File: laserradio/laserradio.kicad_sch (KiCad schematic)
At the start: 60 parts, among them J1 USB4105-GF-A, J3 DEBUG, J4 RIGHT, U1 W25Q128JV, U2 RP2040, U3 MCP1702T-3302E_CB, U4 Opamp_Quad, U5 RS2255, U6 AD9837, Y1 12MHz

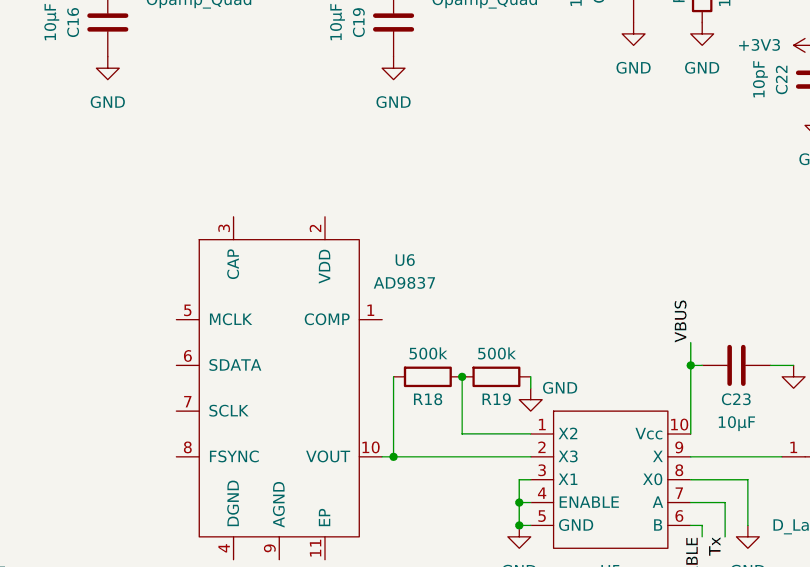
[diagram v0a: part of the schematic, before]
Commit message: swap AD9833 (higher frequency DDS) for AD9837 (lower frequency)
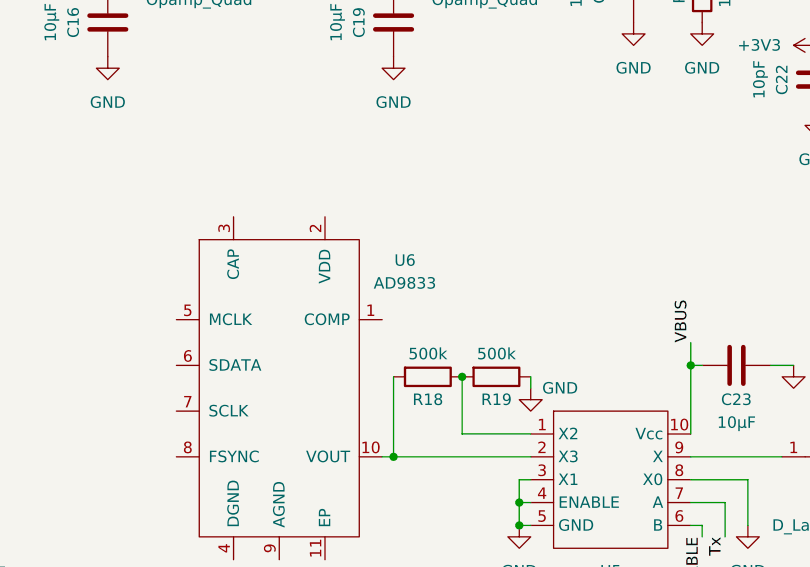
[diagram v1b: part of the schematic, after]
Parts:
- U6: value AD9837 -> AD9833; footprint (none) -> Package_SO:MSOP-10_3x3mm_P0.5mm
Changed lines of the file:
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@@
     (in_bom yes) (on_board yes) (fields_autoplaced)
     (property "Reference" "U6" (id 0) (at 248.92 110.2612 0))
-    (property "Value" "AD9837" (id 1) (at 248.92 112.8012 0))
-    (property "Footprint" "" (id 2) (at 234.95 124.46 0)
-      (effects (font (size 1.27 1.27)) hide)
-    )
-    (property "Datasheet" "" (id 3) (at 234.95 124.46 0)
+    (property "Value" "AD9833" (id 1) (at 248.92 112.8012 0))
+    (property "Footprint" "Package_SO:MSOP-10_3x3mm_P0.5mm" (id 2) (at 234.95 124.46 0)
+      (effects (font (size 1.27 1.27)) hide)
+    )
+    (property "Datasheet" "https://www.analog.com/media/en/technical-documentation/data-sheets/AD9833.pdf" (id 3) (at 234.95 124.46 0)
       (effects (font (size 1.27 1.27)) hide)
     )
@@
     )
     (path "/17770b98-3f4d-46ce-be33-3af9bb07813a"
-      (reference "U6") (unit 1) (value "AD9837") (footprint "")
+      (reference "U6") (unit 1) (value "AD9833") (footprint "Package_SO:MSOP-10_3x3mm_P0.5mm")
     )
     (path "/afdcf360-2e63-4a79-8740-961083c3aaf6"

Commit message: modify 10MHz generator circuit
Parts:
- removed R18, R19: 500k, Resistor_SMD:R_0402_1005Metric, symbol Device:R
- added C?: 100n, symbol Device:C
- added R? (x2): 10k, symbol Device:R
- added U? (x5): Opamp_Quad, symbol Device:Opamp_Quad
- added X?: ASE-xxxMHz, symbol Oscillator:ASE-xxxMHz
- U6: symbol Eclectronics:AD9837 -> Eclectronics:AD9833
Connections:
- net +3V3: now also U6.2 (VDD), X?.1 (EN), X?.4 (Vdd)
- net GND: now also U6.4 (DGND), U6.9 (AGND), C?.2, R?.2, U?.11 (V-), X?.2 (GND)
- net GPIO13: now also U6.8 (FSYNC)
- net GPIO14: now also U6.7 (SCLK)
- net GPIO15: now also U6.6 (SDATA)
- net GPIO29: now also U?.6 (-), U?.7; no longer C21.1, D3.1 (K), R16.2, U4.12 (+)
- net VBUS: now also U?.4 (V+)
- net at U6.10 (VOUT): now also U?.3 (+); no longer U5.2 (X3)
- net at U6.3 (CAP): now also C?.1
- net at U6.5 (MCLK): now also X?.3 (OUT)
- net at U5.1 (X2): now also R?.1, U?.1
- new net: R?.1, R?.2, U5.2 (X3), U?.2 (-)
- new net PEAK_DETECTOR_ANALOG: C21.1, D3.1 (K), R16.2, U4.12 (+), U?.5 (+)
- no-connect marks 15 -> 18
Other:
- note added: "2.5V DAC"
- moved on the sheet: C23, J4, LD1, R17, U5

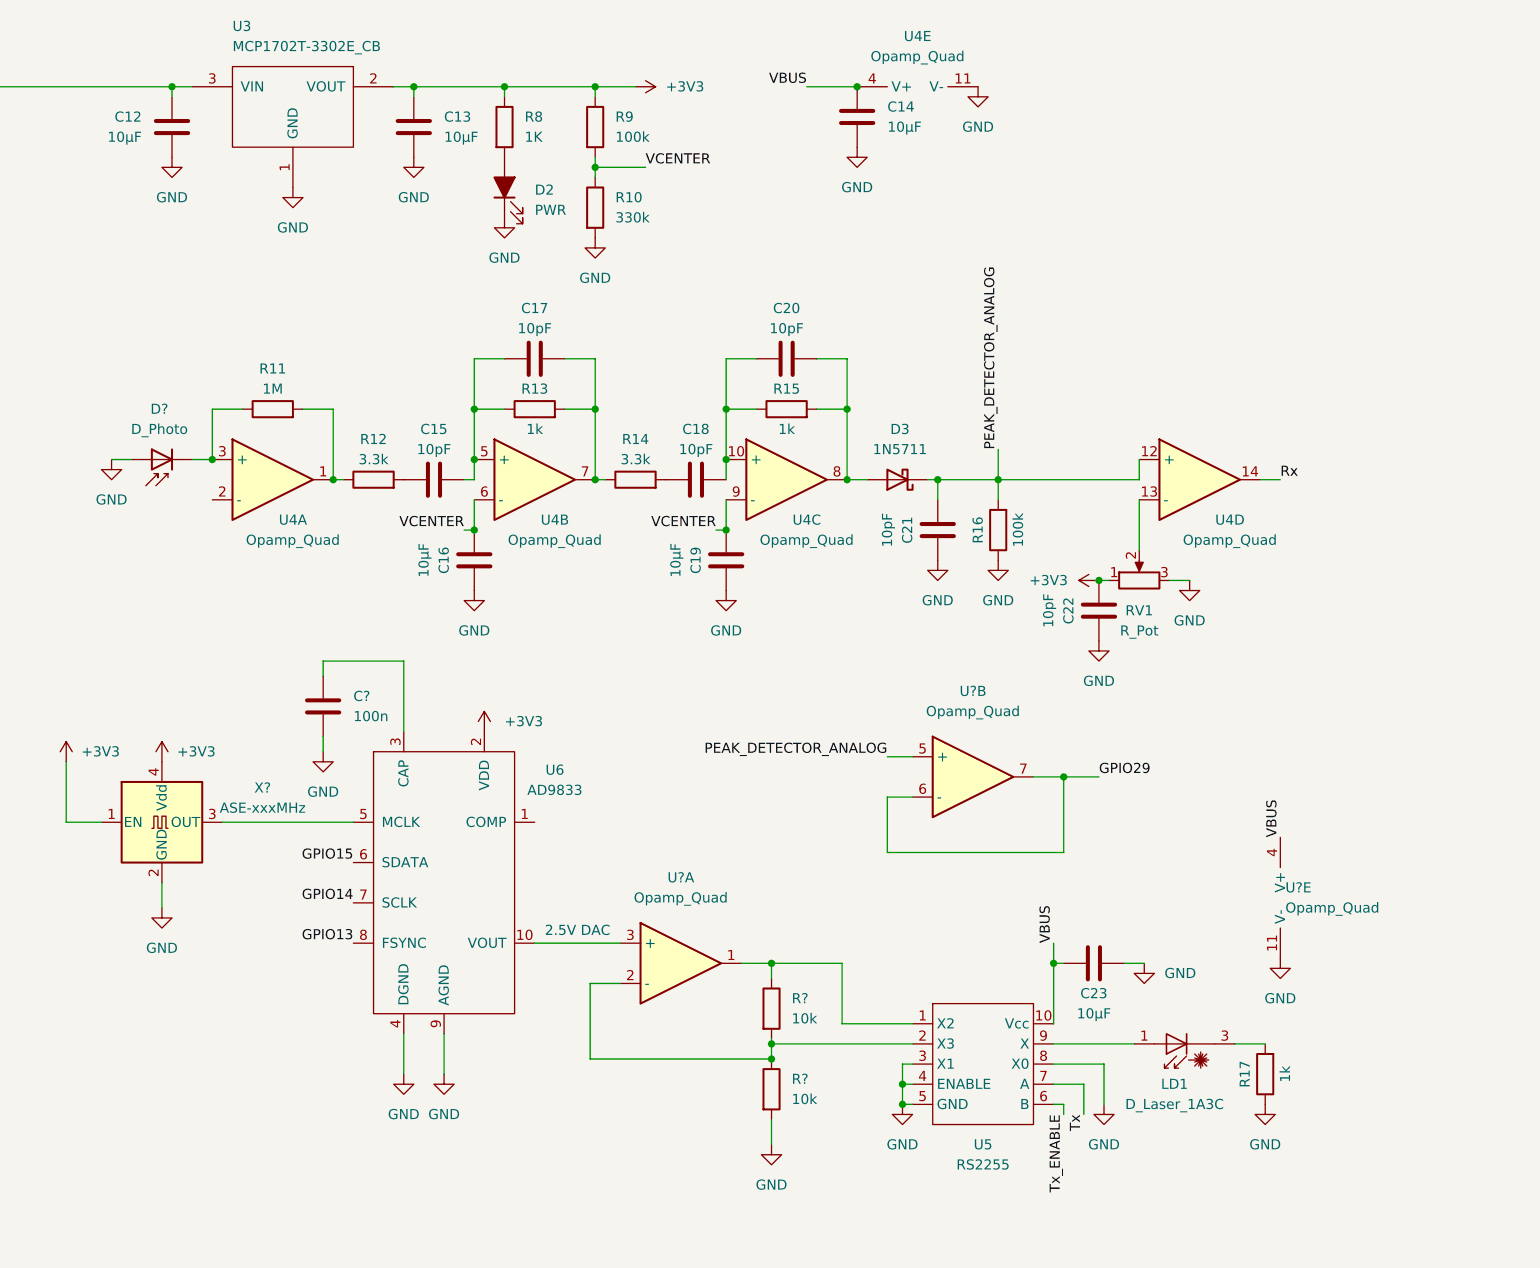
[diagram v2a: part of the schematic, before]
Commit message: finish connecting pins on DDS
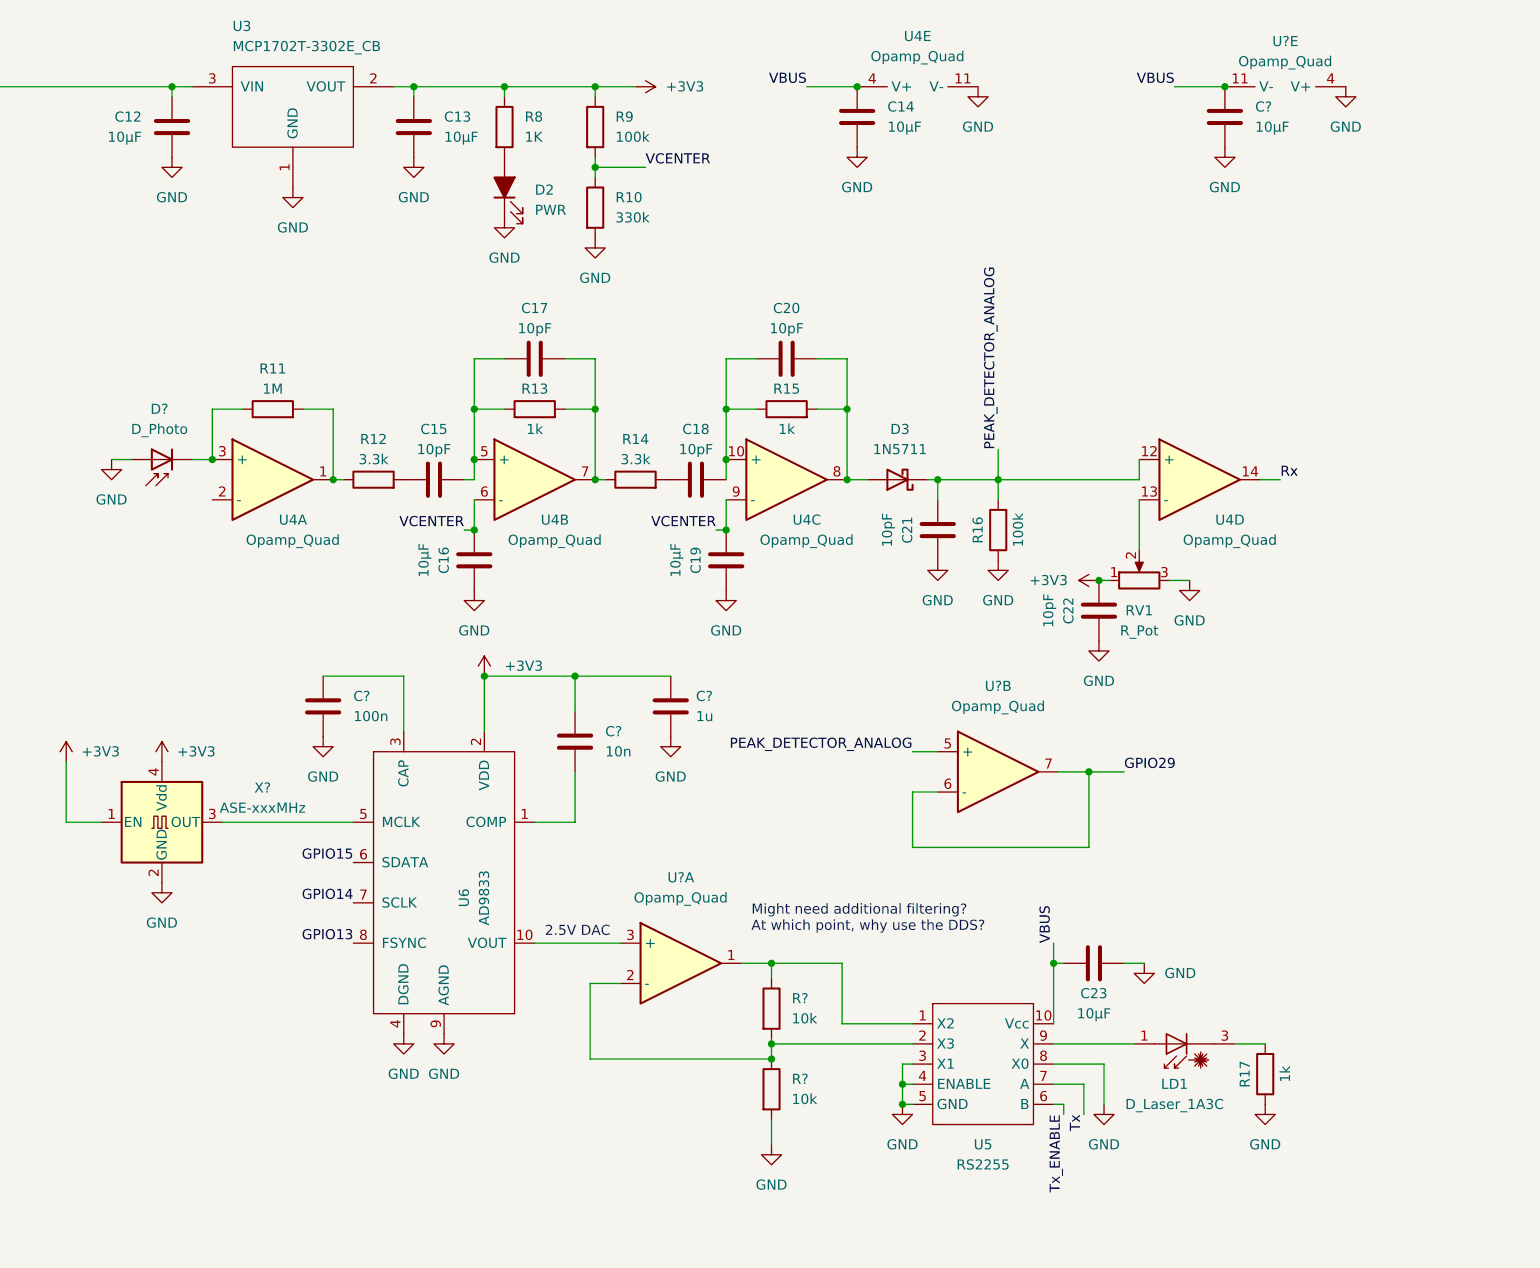
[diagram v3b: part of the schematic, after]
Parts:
- added C?: 10µF, Capacitor_SMD:C_0603_1608Metric, symbol Device:C
- added C?: 10n, symbol Device:C
- added C?: 1u, symbol Device:C
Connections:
- net +3V3: now also C?.1, C?.1
- net GND: now also U?.4 (V+), C?.2, C?.2; no longer U?.11 (V-)
- net VBUS: now also U?.11 (V-), C?.1; no longer U?.4 (V+)
- net at U6.1 (COMP): now also C?.2
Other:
- note added: "Might need additional filtering? At which point, why use the DDS?"
- moved on the sheet: U?B, U?E

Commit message: Uploaded in-class work 11/08/22
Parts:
- removed C?: 10n, symbol Device:C
- removed C?: 100n, symbol Device:C
- removed C?: 1u, symbol Device:C
- removed R11: 1M, Resistor_SMD:R_0402_1005Metric, symbol Device:R
- removed U6: AD9833, Package_SO:MSOP-10_3x3mm_P0.5mm, symbol Eclectronics:AD9833
- added C25: 10µF, Capacitor_SMD:C_0603_1608Metric, symbol Device:C
- added C?: 10pF, symbol Device:C
- added D? (x5): LED, LED_SMD:LED_0805_2012Metric, symbol Device:LED_Filled
- added R?: 1.2k, Resistor_SMD:R_0402_1005Metric, symbol Device:R
- added R? (x5): 1K, Resistor_SMD:R_0402_1005Metric, symbol Device:R
- added RV1: Nominal 1M, symbol Device:R_Potentiometer
- C20: value 10pF -> 1pF
- R15: value 1k -> 10k
- RV2: renamed from RV1; value R_Pot -> Nominal 10k
- gave numbers to parts that had none: 6
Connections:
- net +3V3: now also C25.1
- net GND: now also U4.2 (-), C25.2, D?.1 (K), D?.1 (K), D?.1 (K), D?.1 (K), D?.1 (K)
- net GPIO10: now also R?.1
- net GPIO11: now also R?.1
- net GPIO12: now also R?.1
- net GPIO8: now also R?.1
- net GPIO9: now also R?.1
- net at U6.3 (+): now also Y2.3 (OUT), C?.1, R?.1
- net at D4.1 (K), U4.3 (+): now also RV1.2
- net at R12.1, U4.1: now also RV1.1
- net at R19.1, U6.1: now also U5.2 (X3), C?.2, R?.2; no longer U5.1 (X2)
- net at R19.2, R20.1, U6.2 (-): now also U5.1 (X2); no longer U5.2 (X3)
- net PEAK_DETECTOR_ANALOG: no longer names the net of C21.1, D3.1 (K), R16.2, U4.12 (+), U6.5 (+)
- new net: D?.2 (A), R?.2 (x5)
- no-connect marks 18 -> 14
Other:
- note added: "Band Pass Filter [4.82MHz, 15.92MHz] Gain: 0.3030"
- note added: "Band Pass Filter [4.82MHz, 15.92MHz] Gain: 3.0303"
- note added: "RV1 is configured to be a variable resistor"
- note added: "Square wave former [0V, 5V]"
- note removed: "2.5V DAC"
- note removed: "Might need additional filtering? At which point, why use the DDS?"
- moved on the sheet: C23, J3, LD1, R17, R19, R20, U5, U6A, U6B, Y2
